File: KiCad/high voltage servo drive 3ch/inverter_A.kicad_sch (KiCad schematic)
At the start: 50 parts, among them U2 IPM

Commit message: prepare rev0.1 for manufacturing
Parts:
- C1, C19, C2, C3, C4, C5, C6: Generic Allowed? (none) -> yes; LCSC# (none) -> C106205; Manufacturer (none) -> YAGEO; Part number (none) -> CC0402KRX7R9BB102; cost (none) -> 0.001
- C10, C12, C13, C14, C15, C18, C195, C8: Generic Allowed? (none) -> yes; LCSC# (none) -> C105882; Manufacturer (none) -> YAGEO; Part number (none) -> CC0402KRX5R9BB104; cost (none) -> 0.003
- C11, C139, C7, C9: Generic Allowed? (none) -> yes; LCSC# C7393943 -> C50254; Manufacturer (none) -> Samsung Electro-Mechanics; Part number (none) -> CL31B225KBHNNNE; cost (none) -> 0.03
- C128, C129: Generic Allowed? (none) -> yes; LCSC# C473196 -> C7471876; Manufacturer (none) -> KNSCHA; Part number (none) -> 189RV0014; cost (none) -> 0.05
- C136, C16: Generic Allowed? (none) -> yes; Manufacturer (none) -> HUI JU; Part number (none) -> NV1812B104K102CEMN; cost (none) -> 0.1447
- C17, C20: Generic Allowed? (none) -> yes; LCSC# (none) -> C60133; Manufacturer (none) -> YAGEO; Part number (none) -> CC0402KRX7R9BB103; cost (none) -> 0.001
- D1, D2, D3, D4: Generic Allowed? (none) -> yes; LCSC# SMA2Z22A -> C7440711; Manufacturer (none) -> XCH; Part number (none) -> SMA2Z22A; cost (none) -> 0.07
- FB5, FB6: value FerriteBead -> 0; Generic Allowed? (none) -> yes; LCSC# C963878 -> C2907406; Manufacturer (none) -> FOJAN; Part number (none) -> FRC1206P000 TS; cost (none) -> 0.0015
- NT2, NT3, NT4: now not fitted
- R1, R2, R3, R4, R5, R6, R8: value 100 -> 120; Generic Allowed? (none) -> yes; LCSC# (none) -> C114758; Manufacturer (none) -> YAGEO; Part number (none) -> RC0402FR-07120RL; cost (none) -> 0.0008
- R10, R11, R12, R13, R14, R9: Generic Allowed? (none) -> yes, 1% or better; LCSC # C7419996 -> (none); LCSC# (none) -> C7419996; Manufacturer (none) -> FOJAN; Part number (none) -> FRM121WFR005TM; cost (none) -> 0.03
- R138, R7: Generic Allowed? (none) -> yes; LCSC# (none) -> C105873; Manufacturer (none) -> YAGEO; Part number (none) -> RC0402JR-075K1L; cost (none) -> 0.0006
- U2: Manufacturer (none) -> ONSEMI; now not fitted

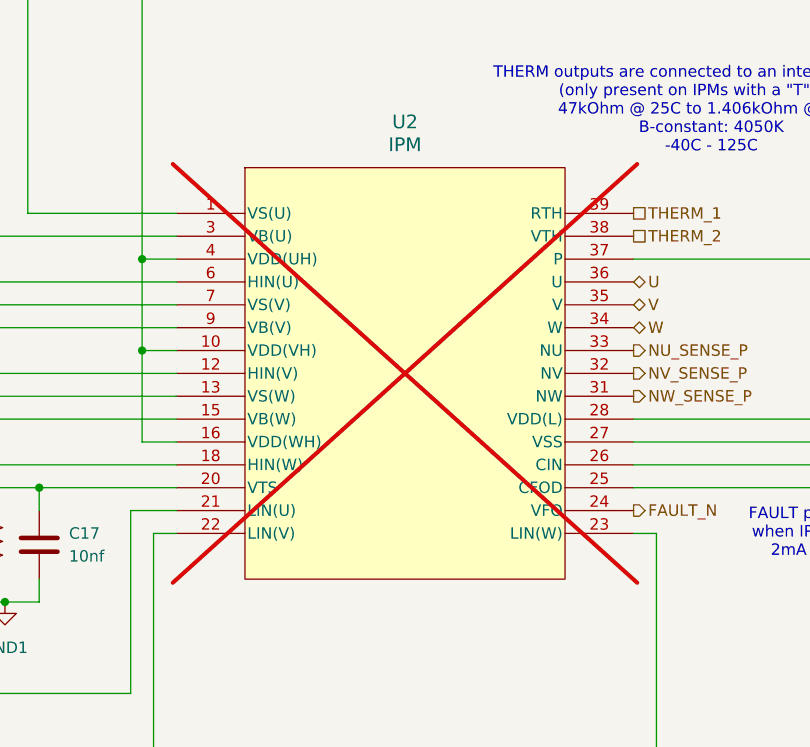
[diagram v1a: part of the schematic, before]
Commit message: update BOM and change transceivers
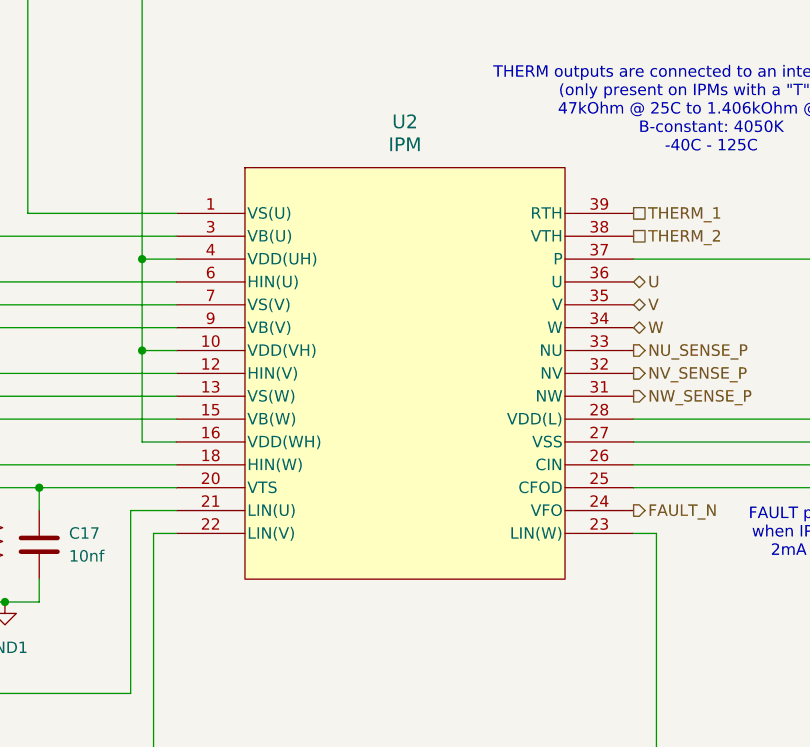
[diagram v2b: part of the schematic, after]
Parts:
- FB5, FB6: LCSC# C2907406 -> C2907288; Part number FRC1206P000 TS -> FRC0805P000 TS
- U2: footprint footprints:DIP39_54.5X31.0_MODGC_OSI -> DIP39_54.5X31.0_MODGC_OSI; now fitted
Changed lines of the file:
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@@
 		(in_bom yes)
 		(on_board yes)
-		(dnp yes)
+		(dnp no)
 		(fields_autoplaced yes)
 		(property "Reference" "U2"
@@
 			)
 		)
-		(property "Footprint" "footprints:DIP39_54.5X31.0_MODGC_OSI"
+		(property "Footprint" "DIP39_54.5X31.0_MODGC_OSI"
 			(at 184.15 121.92 0)
 			(effects
@@
 			)
 		)
-		(property "Datasheet" "IPM"
+		(property "Datasheet" "NFAM3065L4BT"
 			(at 184.15 121.92 0)
 			(effects
@@
 			)
 		)
-		(property "Description" "50v"
+		(property "Description" "Unpolarized capacitor"
 			(at 106.68 157.48 0)
 			(effects
@@
 			)
 		)
-		(property "Description" "50v"
+		(property "Description" "Unpolarized capacitor"
 			(at 116.84 203.2 0)
 			(effects
@@
 			)
 		)
-		(property "Description" "low inductance type"
+		(property "Description" "Resistor, US symbol"
 			(at 344.17 80.01 0)
 			(effects
@@
 			)
 		)
-		(property "Description" "low inductance type"
+		(property "Description" "Resistor, US symbol"
 			(at 344.17 58.42 0)
 			(effects
@@
 			)
 		)
-		(property "Description" "50v"
+		(property "Description" "Unpolarized capacitor"
 			(at 328.93 158.75 0)
 			(effects
@@
 			)
 		)
-		(property "Description" "50v"
+		(property "Description" "Unpolarized capacitor"
 			(at 184.15 85.09 0)
 			(effects
@@
 			)
 		)
-		(property "Description" "63v"
+		(property "Description" "Polarized capacitor"
 			(at 335.28 143.51 0)
 			(effects
@@
 			)
 		)
-		(property "Description" "50v"
+		(property "Description" "Unpolarized capacitor"
 			(at 106.68 203.2 0)
 			(effects
@@
 			)
 		)
-		(property "Description" "50v"
+		(property "Description" "Unpolarized capacitor"
 			(at 184.15 73.66 0)
 			(effects
@@
 			)
 		)
-		(property "Description" "low inductance type"
+		(property "Description" "Resistor, US symbol"
 			(at 344.17 93.98 0)
 			(effects
@@
 			)
 		)
-		(property "Description" "50v"
+		(property "Description" "Unpolarized capacitor"
 			(at 148.59 156.21 0)
 			(effects
@@
 			)
 		)
-		(property "Description" "50v"
+		(property "Description" "Unpolarized capacitor"
 			(at 140.97 85.09 0)
 			(effects
@@
 			)
 		)
-		(property "Description" "50v"
+		(property "Description" "Unpolarized capacitor"
 			(at 184.15 62.23 0)
 			(effects
@@
 			)
 		)
-		(property "Description" "low inductance type"
+		(property "Description" "Resistor, US symbol"
 			(at 344.17 76.2 0)
 			(effects
@@
 			)
 		)
-		(property "Description" "50v"
+		(property "Description" "Unpolarized capacitor"
 			(at 152.4 85.09 0)
 			(effects
@@
 			)
 		)
-		(property "Description" "50v"
+		(property "Description" "Unpolarized capacitor"
 			(at 323.85 143.51 0)
 			(effects
@@
 			)
 		)
-		(property "Description" "50v"
+		(property "Description" "Unpolarized capacitor"
 			(at 316.23 143.51 0)
 			(effects
@@
 			)
 		)
-		(property "LCSC#" "C2907406"
+		(property "LCSC#" "C2907288"
 			(at 316.23 134.62 0)
 			(effects
@@
 			)
 		)
-		(property "Part number" "FRC1206P000 TS"
+		(property "Part number" "FRC0805P000 TS"
 			(at 316.23 134.62 0)
 			(effects
@@
 			)
 		)
-		(property "Description" "50v"
+		(property "Description" "Unpolarized capacitor"
 			(at 163.83 85.09 0)
 			(effects
@@
 			)
 		)
-		(property "Description" "50v"
+		(property "Description" "Unpolarized capacitor"
 			(at 96.52 157.48 0)
 			(effects
@@
 			)
 		)
-		(property "Description" "50v"
+		(property "Description" "Unpolarized capacitor"
 			(at 152.4 73.66 0)
 			(effects
@@
 			)
 		)
-		(property "Description" "low inductance type"
+		(property "Description" "Resistor, US symbol"
 			(at 344.17 97.79 0)
 			(effects
@@
 			)
 		)
-		(property "Description" "50v"
+		(property "Description" "Unpolarized capacitor"
 			(at 163.83 73.66 0)
 			(effects
@@
 			)
 		)
-		(property "LCSC#" "C2907406"
+		(property "LCSC#" "C2907288"
 			(at 176.53 34.29 0)
 			(effects
@@
 			)
 		)
-		(property "Part number" "FRC1206P000 TS"
+		(property "Part number" "FRC0805P000 TS"
 			(at 176.53 34.29 0)
 			(effects
@@
 			)
 		)
-		(property "Description" "50v"
+		(property "Description" "Unpolarized capacitor"
 			(at 96.52 203.2 0)
 			(effects
@@
 			)
 		)
-		(property "Description" "1kv"
+		(property "Description" "Unpolarized capacitor"
 			(at 280.67 124.46 0)
 			(effects
@@
 			)
 		)
-		(property "Description" "50v"
+		(property "Description" "Unpolarized capacitor"
 			(at 307.34 168.91 0)
 			(effects
@@
 			)
 		)
-		(property "Description" "50v"
+		(property "Description" "Unpolarized capacitor"
 			(at 140.97 73.66 0)
 			(effects
@@
 			)
 		)
-		(property "Description" "50v"
+		(property "Description" "Unpolarized capacitor"
 			(at 168.91 158.75 0)
 			(effects
@@
 			)
 		)
-		(property "Description" "1kv"
+		(property "Description" "Unpolarized capacitor"
 			(at 293.37 124.46 0)
 			(effects
@@
 			)
 		)
-		(property "Description" "low inductance type"
+		(property "Description" "Resistor, US symbol"
 			(at 344.17 62.23 0)
 			(effects
@@
 			)
 		)
-		(property "Description" "50v"
+		(property "Description" "Unpolarized capacitor"
 			(at 116.84 157.48 0)
 			(effects
@@
 			)
 		)
-		(property "Description" "63v"
+		(property "Description" "Polarized capacitor"
 			(at 184.15 49.53 0)
 			(effects
